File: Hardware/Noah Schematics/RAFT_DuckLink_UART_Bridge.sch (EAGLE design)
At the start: 9 parts, among them J1 Micro-USB, U1 INTERFACE-CP2102-GMR(QFN28), U2 SP0503BAHT

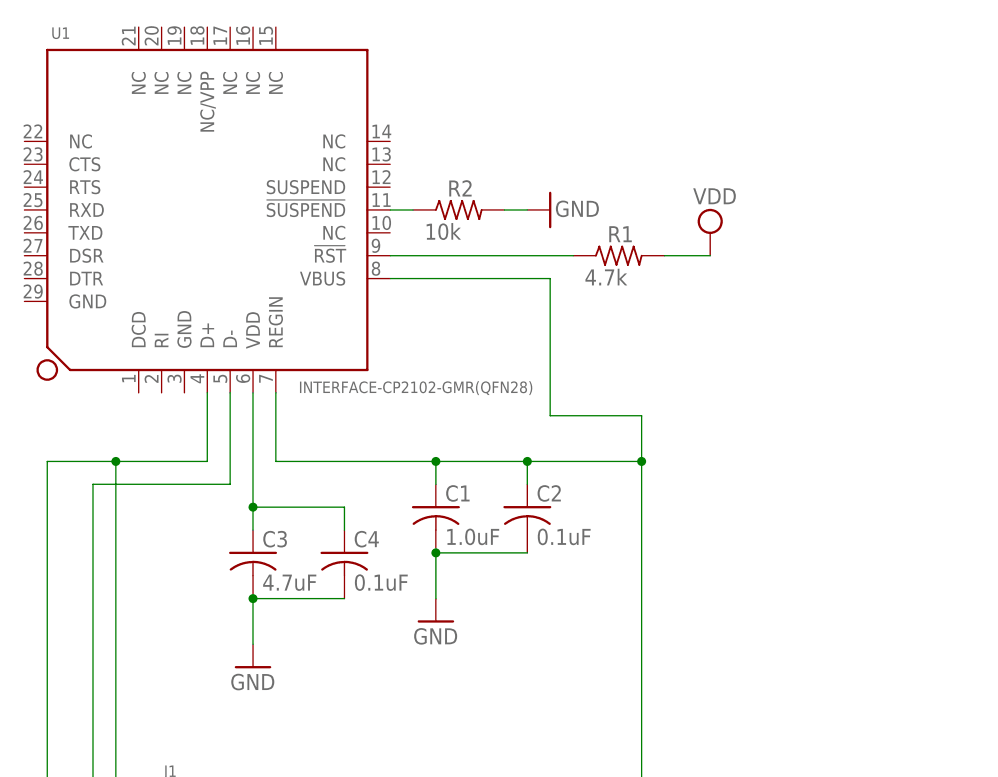
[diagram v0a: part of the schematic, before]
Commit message: Updated UART Bridge with specific components
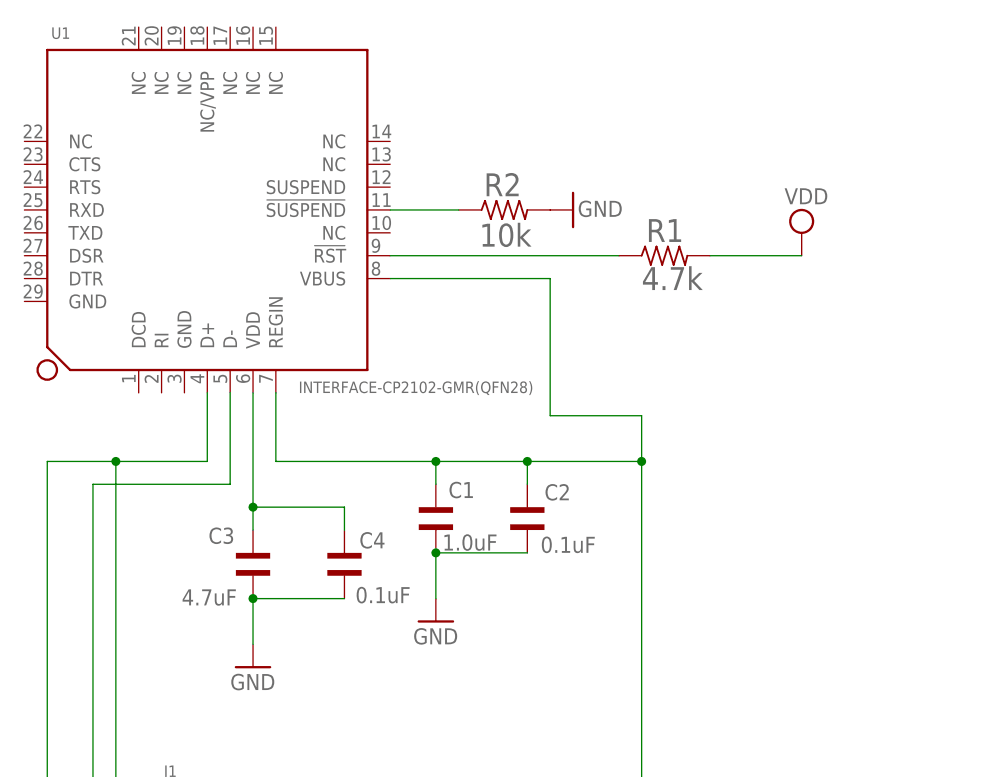
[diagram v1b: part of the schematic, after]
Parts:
- C1: device resistor:C-USC0402 -> GCM155C71A105KE38D:GCM155C71A105KE38D
- C2, C4: device resistor:C-USC0402 -> GRM155R71C104KA88D:GRM155R71C104KA88D
- C3: device resistor:C-USC0402 -> GRM155R60J475ME87D:GRM155R60J475ME87D
- R1: device resistor:R-US_R0402 -> CRCW04024K70JNEDC:CRCW04024K70JNEDC
- R2: device resistor:R-US_R0402 -> CRCW040210K0JNED:CRCW040210K0JNED
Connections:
- net GND: now also C1.1, C2.1, C3.1, C4.1; no longer C1.2, C2.2, C3.2, C4.2
- net N$3: now also C1.2, C2.2; no longer C1.1, C2.1
- net N$4: now also C3.2, C4.2; no longer C3.1, C4.1
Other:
- moved on the sheet: R1, R2
